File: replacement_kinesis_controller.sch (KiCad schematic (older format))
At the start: 72 parts

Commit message: Add voltage regulation
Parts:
- added C? (x2): 4.7uF, symbol CP
- added D?: DIODESCH, symbol DIODESCH
- added Q?: MOS_P, symbol MOS_P
- added R?: 15k, symbol R
- added U?: MCP1700, symbol MCP1700
- R?: value R -> 100k
- R?: value R -> 10k
- R?: value R -> 33k
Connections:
- net +5V: now also D?.1 (A), Q?.G, R?.2
- net +BATT: now also Q?.S
- net GND: now also C?.2, C?.2, R?.1, U?.GND
- net VCC: now also C?.1, U?.VO
- net at CN?.~ (VBUS), CN?.~ (VBUS): now also K?.2 (PM); no longer K?.1 (P1)
- new net: CN?.~ (VBUS), CN?.~ (VBUS), K?.1 (P1) (x2)
- new net: CN?.~ (VBUS), CN?.~ (VBUS), K?.2 (PM)
- new net: C?.1, D?.2 (K), Q?.D, U?.VI
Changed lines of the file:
@@
 P 13200 -1050
 F 0 "R?" V 13280 -1050 40  0000 C CNN
-F 1 "R" V 13207 -1049 40  0000 C CNN
+F 1 "100k" V 13207 -1049 40  0000 C CNN
 F 2 "" V 13130 -1050 30  0000 C CNN
 F 3 "" H 13200 -1050 30  0000 C CNN
@@
 P 13700 -350
 F 0 "R?" V 13780 -350 40  0000 C CNN
-F 1 "R" V 13707 -349 40  0000 C CNN
+F 1 "10k" V 13707 -349 40  0000 C CNN
 F 2 "" V 13630 -350 30  0000 C CNN
 F 3 "" H 13700 -350 30  0000 C CNN
@@
 P 13700 150
 F 0 "R?" V 13780 150 40  0000 C CNN
-F 1 "R" V 13707 151 40  0000 C CNN
+F 1 "33k" V 13707 151 40  0000 C CNN
 F 2 "" V 13630 150 30  0000 C CNN
 F 3 "" H 13700 150 30  0000 C CNN
@@
 Wire Wire Line
 	13700 400  13700 500
+$Comp
+L MOS_P Q?
+U 1 1 54D7AB41
+P 13300 -2700
+F 0 "Q?" H 13300 -2510 60  0000 R CNN
+F 1 "MOS_P" H 13300 -2880 60  0000 R CNN
+F 2 "" H 13300 -2700 60  0000 C CNN
+F 3 "" H 13300 -2700 60  0000 C CNN
+	1    13300 -2700
+	0    1    1    0
+$EndComp
+$Comp
+L +BATT #PWR?
+U 1 1 54D7AC32
+P 12700 -2700
+F 0 "#PWR?" H 12700 -2750 20  0001 C CNN
+F 1 "+BATT" H 12700 -2600 30  0000 C CNN
+F 2 "" H 12700 -2700 60  0000 C CNN
+F 3 "" H 12700 -2700 60  0000 C CNN
+	1    12700 -2700
+	1    0    0    -1
+$EndComp
+$Comp
+L CP C?
+U 1 1 54D7ACD3
+P 13900 -2300
+F 0 "C?" H 13950 -2200 40  0000 L CNN
+F 1 "4.7uF" H 13950 -2400 40  0000 L CNN
+F 2 "" H 14000 -2450 30  0000 C CNN
+F 3 "" H 13900 -2300 300 0000 C CNN
+	1    13900 -2300
+	1    0    0    -1
+$EndComp
+$Comp
+L DIODESCH D?
+U 1 1 54D7AD3B
+P 13700 -3100
+F 0 "D?" H 13700 -3000 40  0000 C CNN
+F 1 "DIODESCH" H 13700 -3200 40  0000 C CNN
+F 2 "" H 13700 -3100 60  0000 C CNN
+F 3 "" H 13700 -3100 60  0000 C CNN
+	1    13700 -3100
+	1    0    0    -1
+$EndComp
+$Comp
+L MCP1700 U?
+U 1 1 54D7B142
+P 14600 -2550
+F 0 "U?" H 14750 -2746 60  0000 C CNN
+F 1 "MCP1700" H 14600 -2350 60  0000 C CNN
+F 2 "" H 14600 -2550 60  0000 C CNN
+F 3 "" H 14600 -2550 60  0000 C CNN
+	1    14600 -2550
+	1    0    0    -1
+$EndComp
+$Comp
+L VCC #PWR?
+U 1 1 54D7C01B
+P 15300 -2700
+F 0 "#PWR?" H 15300 -2600 30  0001 C CNN
+F 1 "VCC" H 15300 -2600 30  0000 C CNN
+F 2 "" H 15300 -2700 60  0000 C CNN
+F 3 "" H 15300 -2700 60  0000 C CNN
+	1    15300 -2700
+	1    0    0    -1
+$EndComp
+Wire Wire Line
+	13500 -2600 14200 -2600
+Wire Wire Line
+	13900 -3100 13900 -2500
+Connection ~ 13900 -2600
+Wire Wire Line
+	12700 -2700 12700 -2600
+Wire Wire Line
+	12700 -2600 13100 -2600
+Wire Wire Line
+	13300 -2900 13300 -3100
+Wire Wire Line
+	12400 -3100 13500 -3100
+$Comp
+L +5V #PWR?
+U 1 1 54D7DD8E
+P 12700 -3200
+F 0 "#PWR?" H 12700 -3110 20  0001 C CNN
+F 1 "+5V" H 12700 -3110 30  0000 C CNN
+F 2 "" H 12700 -3200 60  0000 C CNN
+F 3 "" H 12700 -3200 60  0000 C CNN
+	1    12700 -3200
+	1    0    0    -1
+$EndComp
+Wire Wire Line
+	12700 -3200 12700 -3100
+Connection ~ 13300 -3100
+Wire Wire Line
+	15000 -2600 15300 -2600
+Wire Wire Line
+	15300 -2700 15300 -2500
+$Comp
+L GND #PWR?
+U 1 1 54D812AC
+P 14600 -2000
+F 0 "#PWR?" H 14600 -2000 30  0001 C CNN
+F 1 "GND" H 14600 -2070 30  0001 C CNN
+F 2 "" H 14600 -2000 60  0000 C CNN
+F 3 "" H 14600 -2000 60  0000 C CNN
+	1    14600 -2000
+	1    0    0    -1
+$EndComp
+Wire Wire Line
+	12400 -2100 15300 -2100
+Wire Wire Line
+	14600 -2300 14600 -2000
+Connection ~ 14600 -2100
+$Comp
+L R R?
+U 1 1 54D817BA
+P 12400 -2550
+F 0 "R?" V 12480 -2550 40  0000 C CNN
+F 1 "15k" V 12407 -2549 40  0000 C CNN
+F 2 "" V 12330 -2550 30  0000 C CNN
+F 3 "" H 12400 -2550 30  0000 C CNN
+	1    12400 -2550
+	-1   0    0    1
+$EndComp
+Wire Wire Line
+	12400 -2800 12400 -3100
+Connection ~ 12700 -3100
+Wire Wire Line
+	12400 -2300 12400 -2100
+Connection ~ 13900 -2100
+$Comp
+L CP C?
+U 1 1 54D83C87
+P 15300 -2300
+F 0 "C?" H 15350 -2200 40  0000 L CNN
+F 1 "4.7uF" H 15350 -2400 40  0000 L CNN
+F 2 "" H 15400 -2450 30  0000 C CNN
+F 3 "" H 15300 -2300 300 0000 C CNN
+	1    15300 -2300
+	1    0    0    -1
+$EndComp
+Connection ~ 15300 -2600
 $EndSCHEMATC

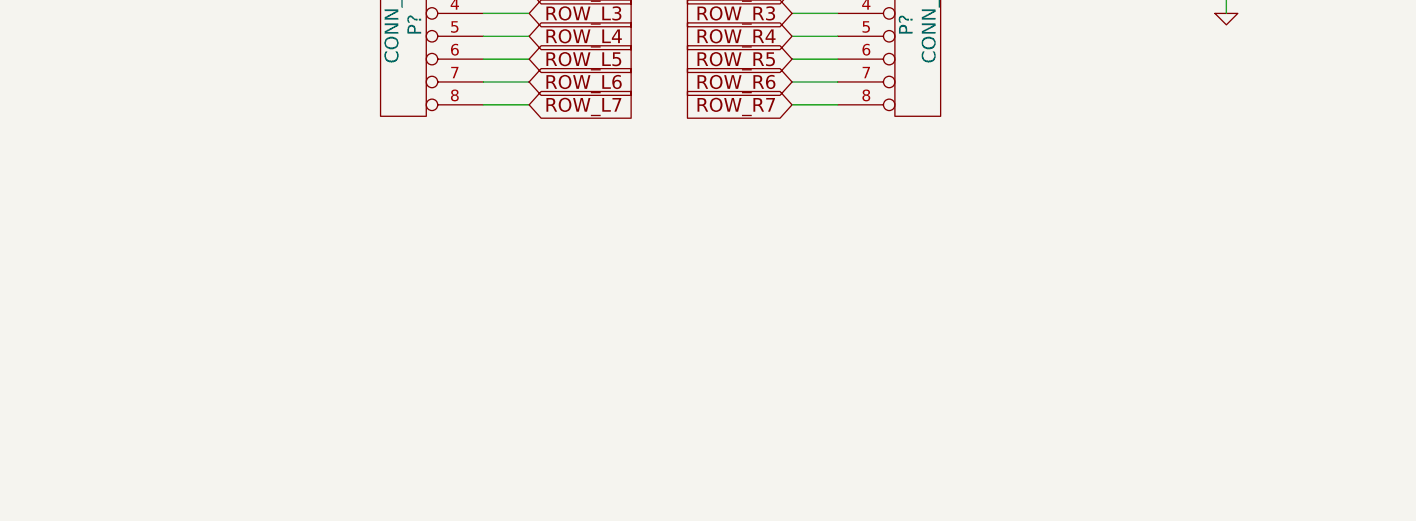
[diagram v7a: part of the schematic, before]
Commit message: Add breakouts for empty sections of switch matrix
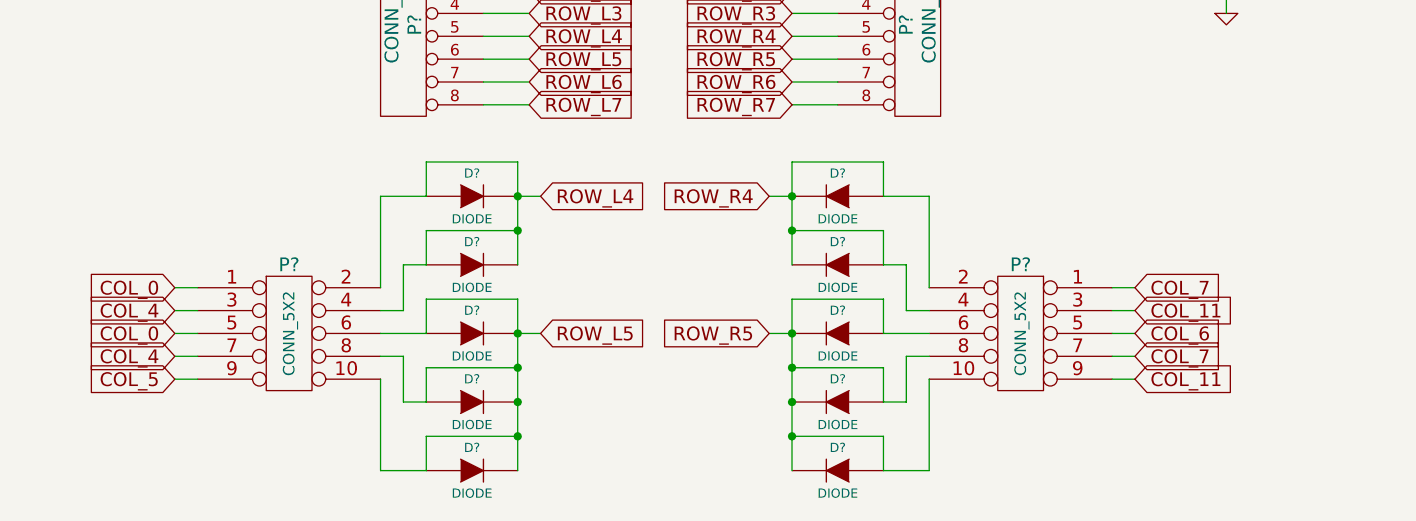
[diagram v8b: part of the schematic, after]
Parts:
- added D? (x10): DIODE, symbol DIODE
- added P? (x2): CONN_5X2, symbol CONN_5X2
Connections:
- net COL_0: now also P?.1, P?.5
- net COL_11: now also P?.3, P?.9
- net COL_4: now also P?.3, P?.7
- net COL_5: now also P?.9
- net COL_6: now also P?.5
- net COL_7: now also P?.1, P?.7
- net GPA4: now also D?.1 (A), D?.1 (A), D?.2 (K), D?.2 (K), P?.2, P?.4
- net GPA5: now also D?.1 (A), D?.1 (A), D?.1 (A), D?.2 (K), D?.2 (K), D?.2 (K), P?.10, P?.6, P?.8
- net PB4: now also D?.1 (A), D?.1 (A), D?.2 (K), D?.2 (K), P?.2, P?.4
- net PB5: now also D?.1 (A), D?.1 (A), D?.1 (A), D?.2 (K), D?.2 (K), D?.2 (K), P?.10, P?.6, P?.8
- net at CN?.~ (VBUS), CN?.~ (VBUS): now also K?.2 (PM); no longer K?.1 (P1)
- new net: CN?.~ (VBUS), CN?.~ (VBUS), K?.1 (P1) (x2)
- new net: CN?.~ (VBUS), CN?.~ (VBUS), K?.2 (PM)
